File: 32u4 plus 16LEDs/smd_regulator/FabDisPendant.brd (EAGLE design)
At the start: 76.2 x 54.2 mm, 70 parts, among them IC1 MPR121, J2 AVR_SPI_PRG_6PTH, U3 ATMEGA32U4, Y1 16MHz

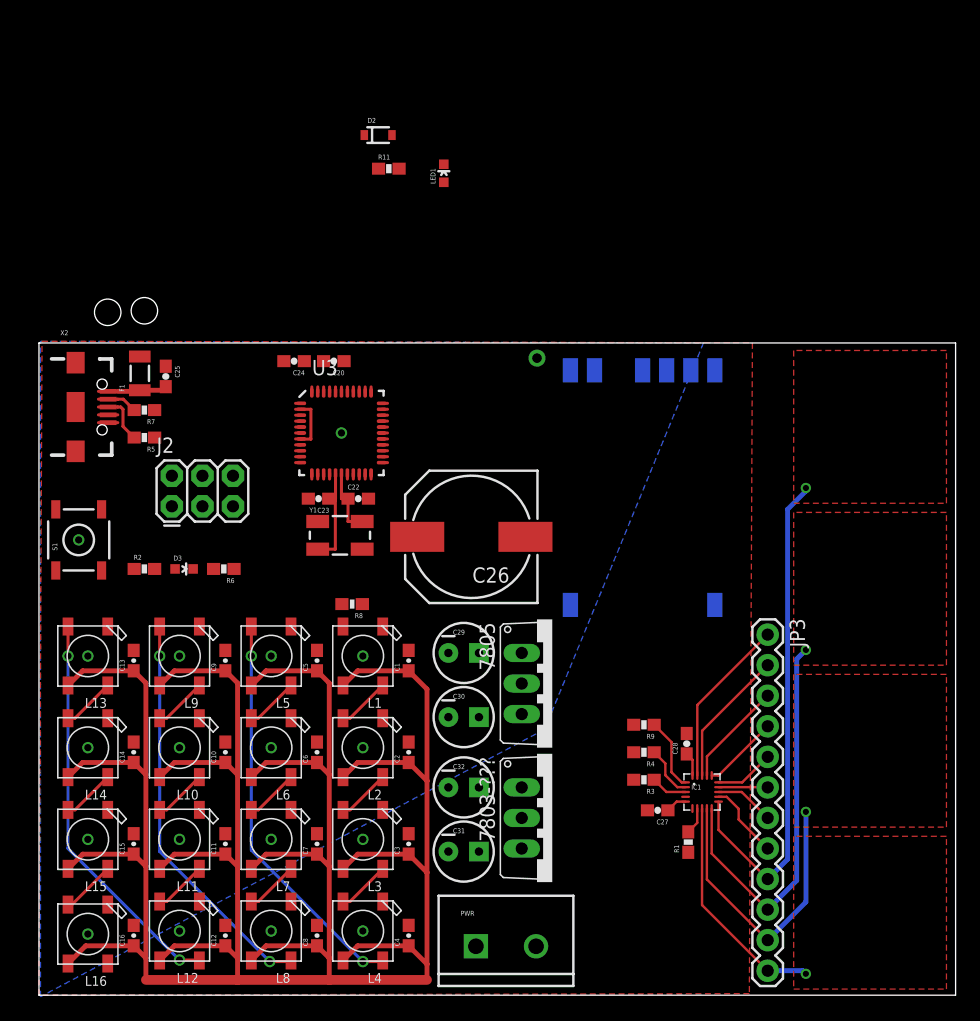
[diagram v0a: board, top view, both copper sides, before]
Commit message: Switch to 7805 regulator
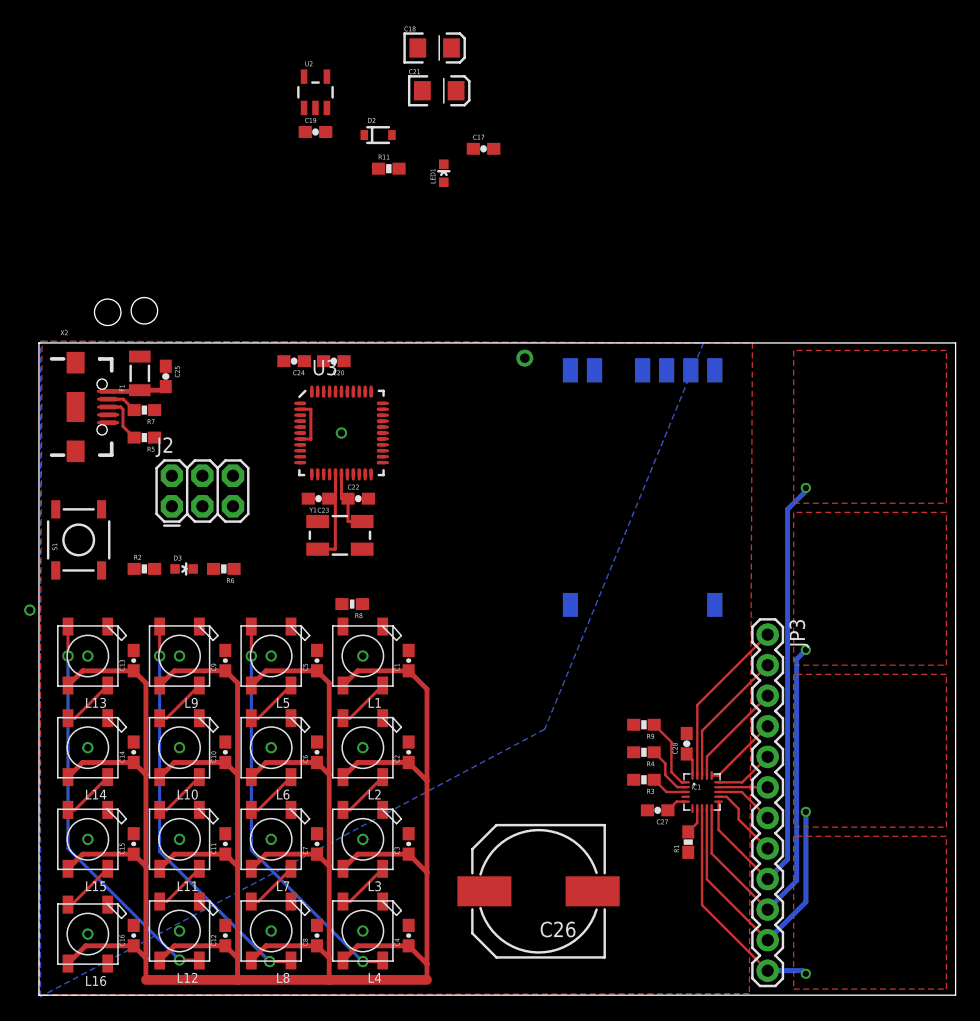
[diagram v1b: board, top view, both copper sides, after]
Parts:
- removed 7803-???, 7805: 7805TV, linear:TO220V
- removed C29, C31: 10uf, SparkFun-Capacitors:CPOL-RADIAL-10UF-25V
- removed C30, C32: 1uf, SparkFun-Capacitors:CPOL-RADIAL-10UF-25V
- removed PWR: M025MM, SparkFun-Connectors:SCREWTERMINAL-5MM-2
- added C17: 1uF, SparkFun:0603-CAP
- added C18, C21: 10uF, SparkFun:EIA3216
- added C19: 0.1uF, SparkFun:0603-CAP
- added U2: MIC5219, SparkFun:SOT23-5
- moved C26 30.0 mm to (41.5, 8.64)
- moved U$1 1.02 mm to (40.4, 53.0)
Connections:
- net 3.3V: no longer 7803-???.2, C32.1
- net 5V: now also C17.1, C18.A, C19.2, U2.5; no longer 7805.3, C30.1
- net GND: now also C17.2, C18.C, C19.1, C21.C, U2.2; no longer 7803-???.1, 7805.2, C29.2, C30.2, C31.2, C32.2, PWR.2
- net RAW: now also C21.A, U2.1, U2.3; no longer 7803-???.3, 7805.1, C29.1, C31.1, PWR.1
